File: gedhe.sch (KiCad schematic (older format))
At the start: 56 parts, among them SW1 switch, SW10 switch, SW11 switch, SW12 switch, SW13 switch, SW14 switch, SW15 switch, SW16 switch, SW17 switch, SW18 switch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

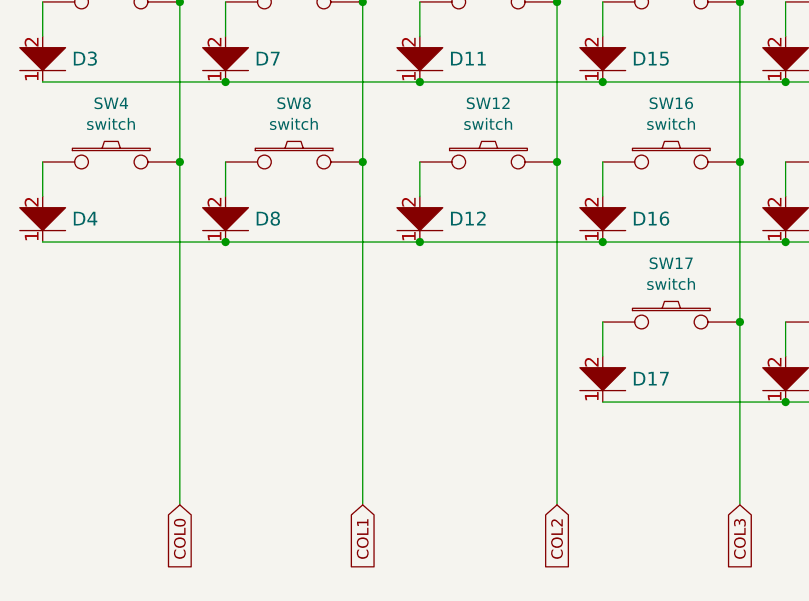
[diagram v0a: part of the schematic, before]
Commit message: 29 keys per side.
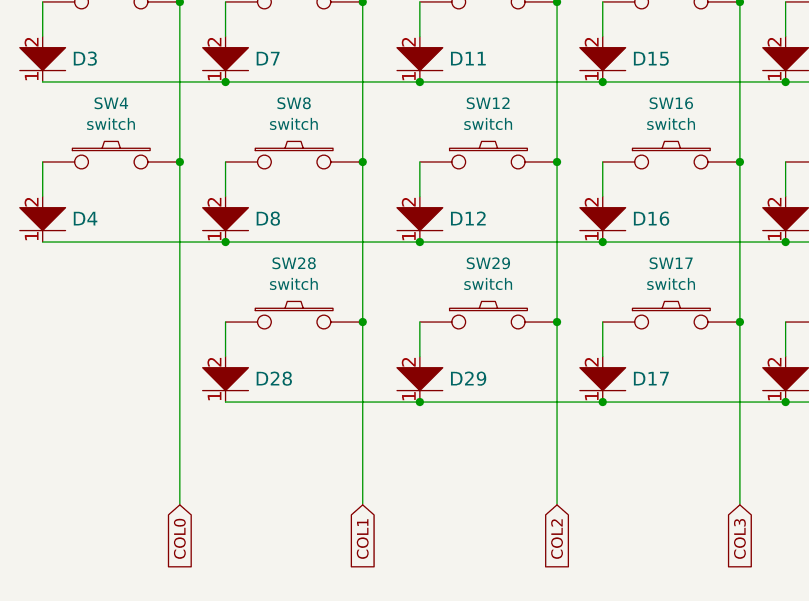
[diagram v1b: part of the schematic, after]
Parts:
- added D28, D29: D, footprints:diode, symbol gedhe:diode
- added SW28, SW29: switch, footprints:1u-dual, symbol gedhe:switch
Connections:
- net COL1: now also SW28.2
- net COL2: now also SW29.2
- net ROW4: now also D28.1, D29.1
- new net: D29.2, SW29.1
- new net: D28.2, SW28.1
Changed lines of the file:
@@
 	3750 3250 4550 3250
 Wire Wire Line
-	3750 3950 4550 3950
+	2100 3950 2950 3950
 Text GLabel 6250 1150 2    50   Input ~ 0
 ROW0
@@
 SDA
 Wire Wire Line
-	3550 2900 3550 4400
-Wire Wire Line
-	2700 2900 2700 4400
+	3550 2900 3550 3600
+Wire Wire Line
+	2700 2900 2700 3600
 NoConn ~ 10525 1125
 Text GLabel 10525 1025 2    50   Input ~ 0
@@
 Text GLabel 7775 1975 0    50   Input ~ 0
 COL5
+$Comp
+L gedhe:switch SW29
+U 1 1 5F8309F0
+P 3250 3600
+F 0 "SW29" H 3250 3855 50  0000 C CNN
+F 1 "switch" H 3250 3764 50  0000 C CNN
+F 2 "footprints:1u-dual" H 3250 3600 60  0001 C CNN
+F 3 "" H 3250 3600 60  0000 C CNN
+	1    3250 3600
+	1    0    0    -1
+$EndComp
+$Comp
+L gedhe:diode D29
+U 1 1 5F830C38
+P 2950 3900
+F 0 "D29" H 2822 3850 60  0000 R CNN
+F 1 "D" V 3100 3850 60  0001 C CNN
+F 2 "footprints:diode" H 2950 3900 60  0001 C CNN
+F 3 "" H 2950 3900 60  0000 C CNN
+	1    2950 3900
+	-1   0    0    1
+$EndComp
+Wire Wire Line
+	2950 3600 2950 3750
+Connection ~ 3550 3600
+Wire Wire Line
+	3550 3600 3550 4400
+$Comp
+L gedhe:switch SW28
+U 1 1 5F83779E
+P 2400 3600
+F 0 "SW28" H 2400 3855 50  0000 C CNN
+F 1 "switch" H 2400 3764 50  0000 C CNN
+F 2 "footprints:1u-dual" H 2400 3600 60  0001 C CNN
+F 3 "" H 2400 3600 60  0000 C CNN
+	1    2400 3600
+	1    0    0    -1
+$EndComp
+$Comp
+L gedhe:diode D28
+U 1 1 5F837922
+P 2100 3900
+F 0 "D28" H 1972 3850 60  0000 R CNN
+F 1 "D" V 2250 3850 60  0001 C CNN
+F 2 "footprints:diode" H 2100 3900 60  0001 C CNN
+F 3 "" H 2100 3900 60  0000 C CNN
+	1    2100 3900
+	-1   0    0    1
+$EndComp
+Wire Wire Line
+	2100 3600 2100 3750
+Connection ~ 2700 3600
+Wire Wire Line
+	2700 3600 2700 4400
+Connection ~ 2950 3950
+Wire Wire Line
+	2950 3950 3750 3950
+Connection ~ 3750 3950
+Wire Wire Line
+	3750 3950 4550 3950
 $EndSCHEMATC

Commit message: added key.
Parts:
- added D30: D, footprints:diode, symbol gedhe:diode
- added SW30: switch, footprints:1u-dual, symbol gedhe:switch
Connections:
- net COL0: now also SW30.2
- net ROW4: now also D30.1
- new net: D30.2, SW30.1
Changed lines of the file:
@@
 COL4
 Wire Wire Line
-	1900 2900 1900 4400
+	1900 2900 1900 3600
 NoConn ~ 7775 1075
 NoConn ~ 7775 1175
@@
 Wire Wire Line
 	3750 3950 4550 3950
+$Comp
+L gedhe:switch SW30
+U 1 1 5F8501A7
+P 1600 3600
+F 0 "SW30" H 1600 3855 50  0000 C CNN
+F 1 "switch" H 1600 3764 50  0000 C CNN
+F 2 "footprints:1u-dual" H 1600 3600 60  0001 C CNN
+F 3 "" H 1600 3600 60  0000 C CNN
+	1    1600 3600
+	1    0    0    -1
+$EndComp
+$Comp
+L gedhe:diode D30
+U 1 1 5F85033B
+P 1300 3900
+F 0 "D30" H 1172 3850 60  0000 R CNN
+F 1 "D" V 1450 3850 60  0001 C CNN
+F 2 "footprints:diode" H 1300 3900 60  0001 C CNN
+F 3 "" H 1300 3900 60  0000 C CNN
+	1    1300 3900
+	-1   0    0    1
+$EndComp
+Wire Wire Line
+	1300 3600 1300 3750
+Connection ~ 1900 3600
+Wire Wire Line
+	1900 3600 1900 4400
+Wire Wire Line
+	1300 3950 2100 3950
+Connection ~ 2100 3950
 $EndSCHEMATC
